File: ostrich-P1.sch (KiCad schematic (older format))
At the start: 112 parts

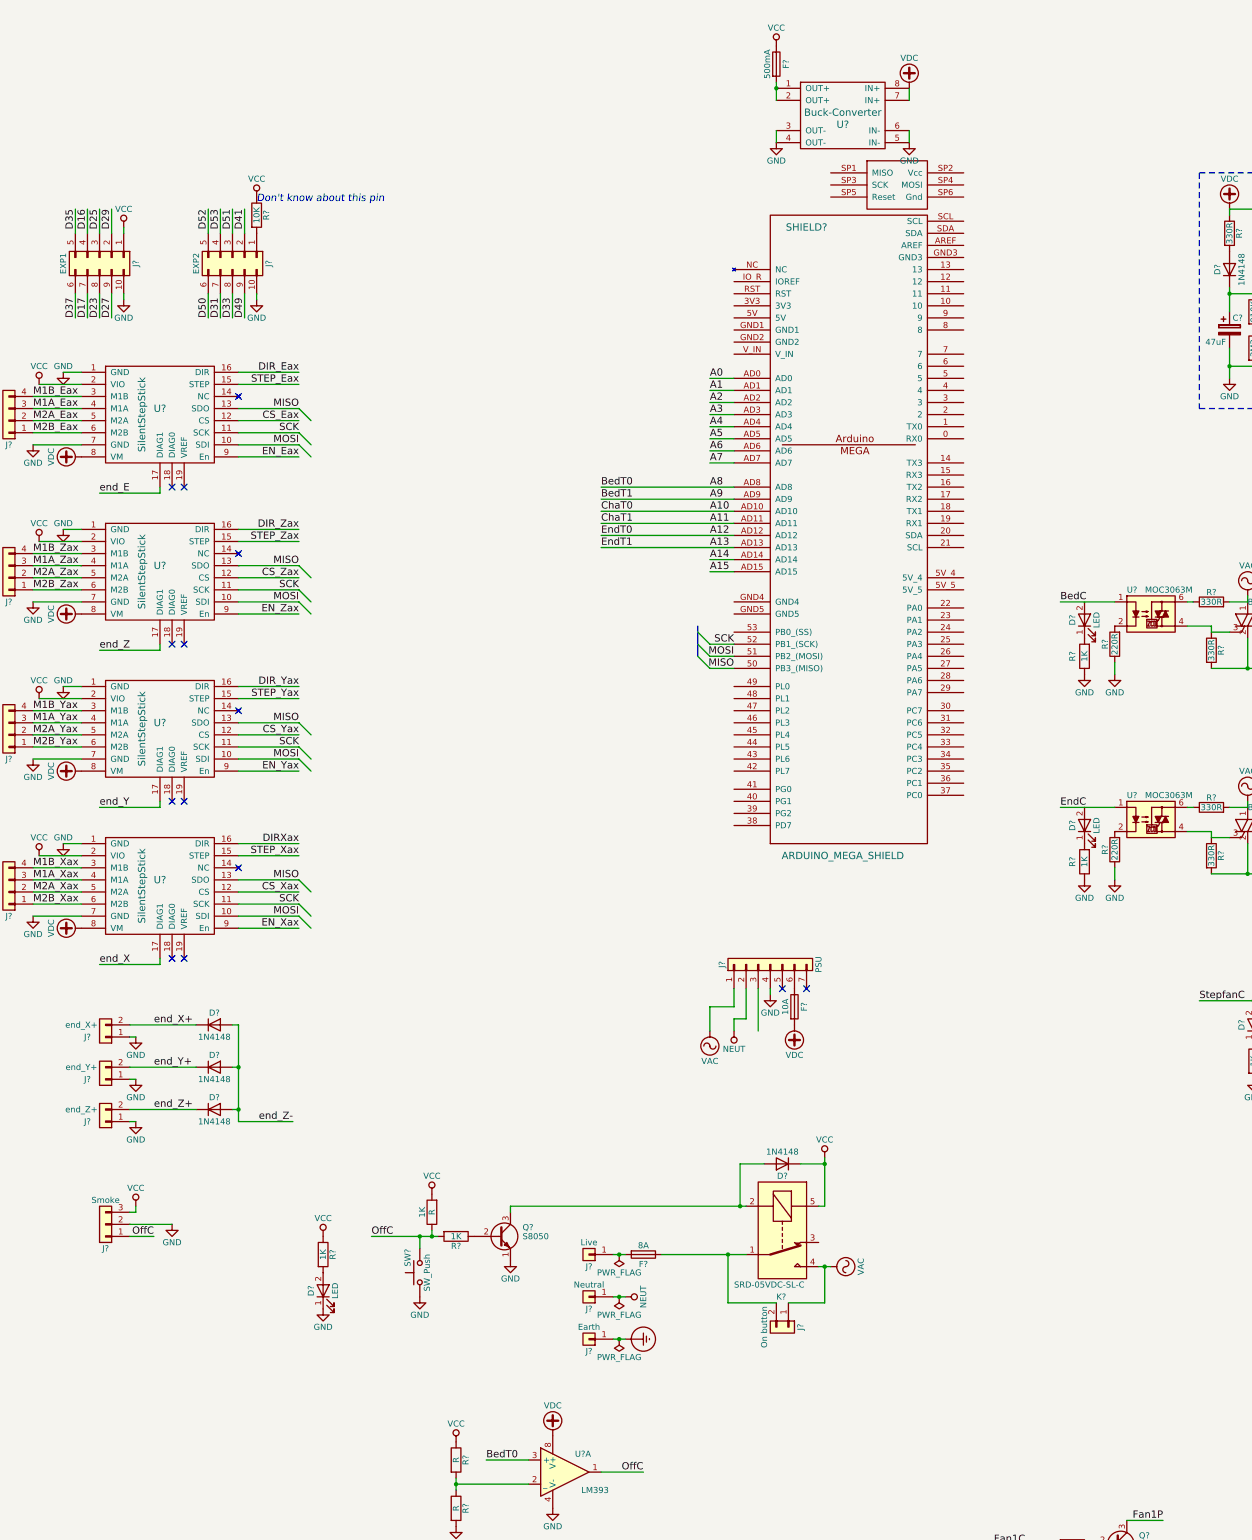
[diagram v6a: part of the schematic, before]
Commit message: switched mega shield library
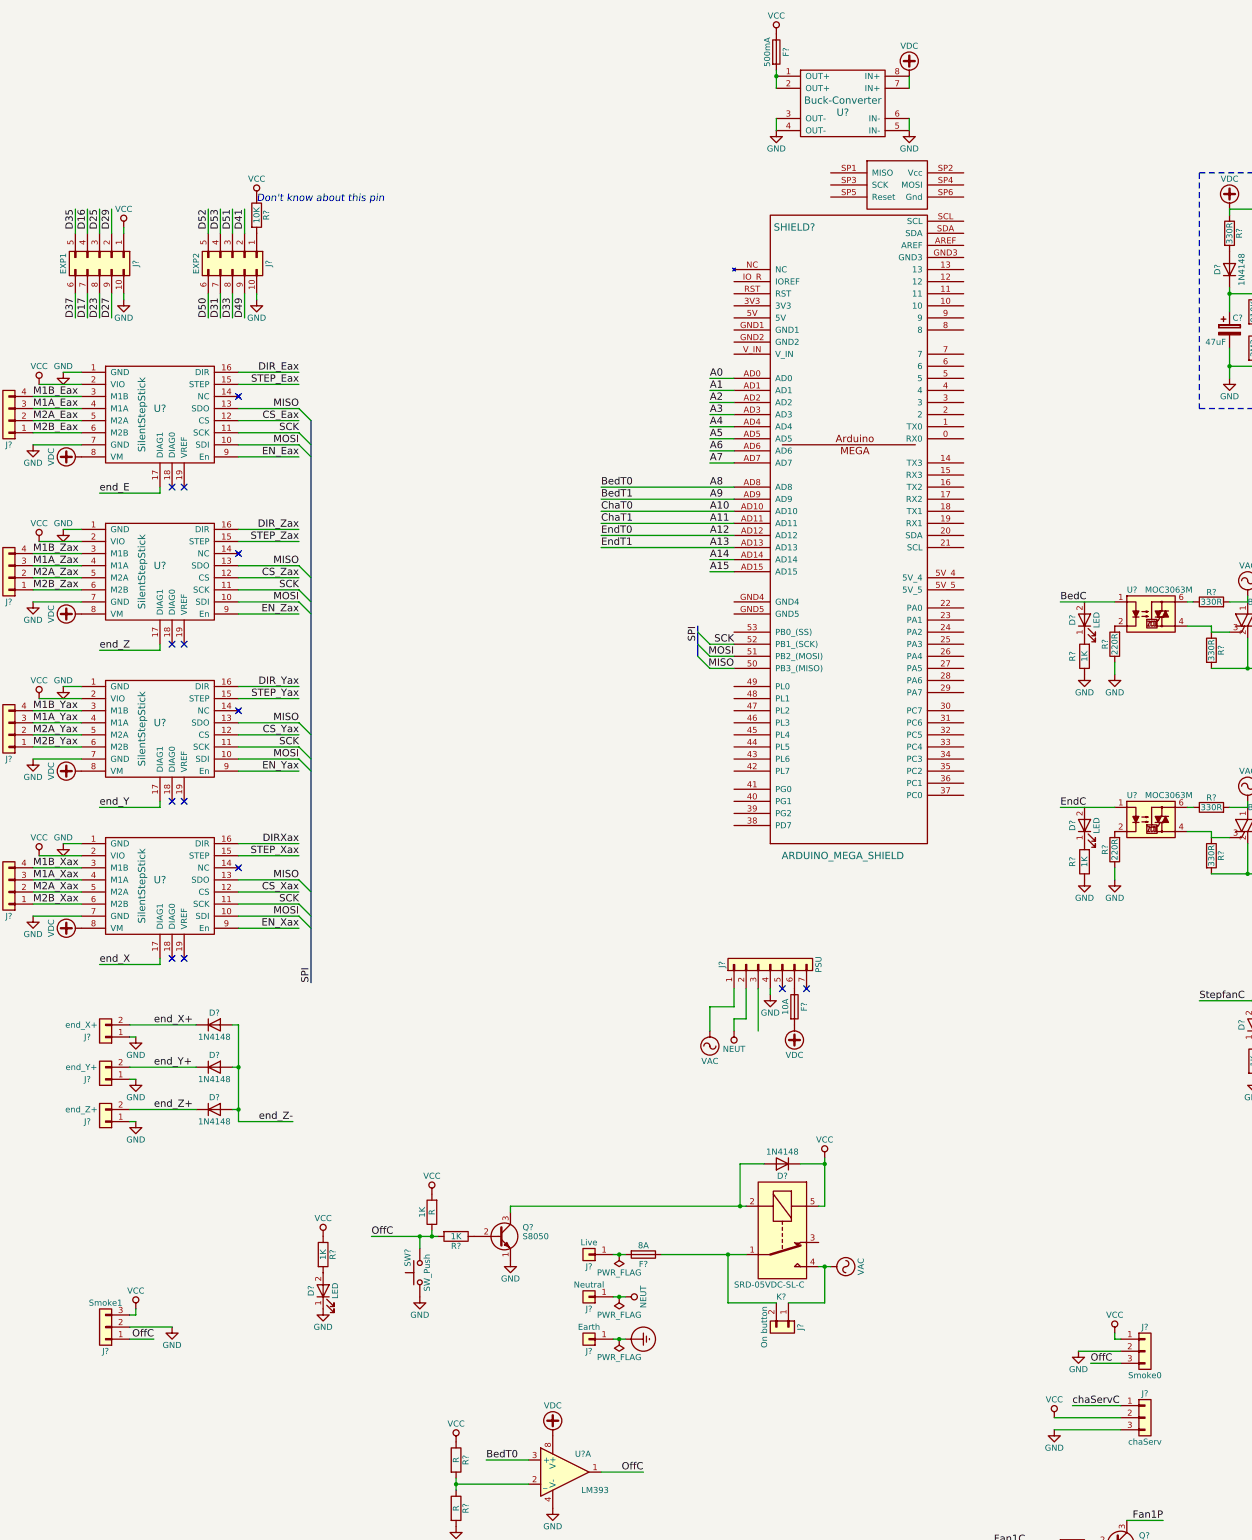
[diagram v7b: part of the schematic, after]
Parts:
- removed SHIELD?: ARDUINO_MEGA_SHIELD, symbol ARDUINO_MEGA_SHIELD
- added J?: Smoke1, symbol Conn_01x03
- added J?: chaServ, symbol Conn_01x03
- added SHIELD?: ARDUINO_MEGA_SHIELD, FT:ARDUINO_MEGA_SHIELD, symbol ARDUINO_MEGA_SHIELD
- J?: value Smoke -> Smoke0
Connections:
- net A0: now also SHIELD?.AD0
- net A1: now also SHIELD?.AD1
- net A10: now also SHIELD?.AD10
- net A11: now also SHIELD?.AD11
- net A12: now also SHIELD?.AD12
- net A13: now also SHIELD?.AD13
- net A14: now also SHIELD?.AD14
- net A15: now also SHIELD?.AD15
- net A2: now also SHIELD?.AD2
- net A3: now also SHIELD?.AD3
- net A4: now also SHIELD?.AD4
- net A5: now also SHIELD?.AD5
- net A6: now also SHIELD?.AD6
- net A7: now also SHIELD?.AD7
- net A8: now also SHIELD?.AD8
- net A9: now also SHIELD?.AD9
- net GND: now also J?.2 (Pin_2), J?.3 (Pin_3)
- net MISO: now also SHIELD?.50 (PB3_(MISO))
- net MOSI: now also SHIELD?.51 (PB2_(MOSI))
- net OffC: now also J?.3 (Pin_3), J?.1 (Pin_1); no longer J?.1 (Pin_1)
- net SCK: now also SHIELD?.52 (PB1_(SCK))
- net VCC: now also J?.1 (Pin_1), J?.2 (Pin_2), J?.3 (Pin_3); no longer J?.3 (Pin_3)
- new net chaServC: J?.1 (Pin_1)
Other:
- moved on the sheet: F?, J?, U?
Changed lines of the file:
@@
 LIBS:contrib
 LIBS:valves
-LIBS:arduino_shieldsNCL
 LIBS:my components
 LIBS:ESP8266
+LIBS:freetronics_schematic
 LIBS:ostrich-P1-cache
 EELAYER 25 0
@@
 $EndDescr
 $Comp
-L ARDUINO_MEGA_SHIELD SHIELD?
-U 1 1 5AF9CD22
-P 6500 3450
-F 0 "SHIELD?" H 6100 5950 60  0000 C CNN
-F 1 "ARDUINO_MEGA_SHIELD" H 6400 750 60  0000 C CNN
-F 2 "" H 6500 3450 60  0001 C CNN
-F 3 "" H 6500 3450 60  0001 C CNN
-	1    6500 3450
-	1    0    0    -1
-$EndComp
-$Comp
 L SilentStepStick U?
 U 1 1 5AF9DD5F
@@
 L Buck-Converter U?
 U 1 1 5AFC21BD
-P 6400 0
-F 0 "U?" H 6400 -100 60  0000 C CNN
-F 1 "Buck-Converter" H 6400 0   60  0000 C CNN
-F 2 "" H 6400 0   60  0001 C CNN
-F 3 "" H 6400 0   60  0001 C CNN
-	1    6400 0
+P 6400 -100
+F 0 "U?" H 6400 -200 60  0000 C CNN
+F 1 "Buck-Converter" H 6400 -100 60  0000 C CNN
+F 2 "" H 6400 -100 60  0001 C CNN
+F 3 "" H 6400 -100 60  0001 C CNN
+	1    6400 -100
 	1    0    0    -1
 $EndComp
@@
 L VDC #PWR030
 U 1 1 5AFC32E0
-P 6950 -200
-F 0 "#PWR030" H 6950 -300 50  0001 C CNN
-F 1 "VDC" H 6950 50  50  0000 C CNN
-F 2 "" H 6950 -200 50  0001 C CNN
-F 3 "" H 6950 -200 50  0001 C CNN
-	1    6950 -200
+P 6950 -300
+F 0 "#PWR030" H 6950 -400 50  0001 C CNN
+F 1 "VDC" H 6950 -50 50  0000 C CNN
+F 2 "" H 6950 -300 50  0001 C CNN
+F 3 "" H 6950 -300 50  0001 C CNN
+	1    6950 -300
 	1    0    0    -1
 $EndComp
@@
 L VCC #PWR031
 U 1 1 5AFC334E
-P 5850 -550
-F 0 "#PWR031" H 5850 -700 50  0001 C CNN
-F 1 "VCC" H 5850 -400 50  0000 C CNN
-F 2 "" H 5850 -550 50  0001 C CNN
-F 3 "" H 5850 -550 50  0001 C CNN
-	1    5850 -550
+P 5850 -650
+F 0 "#PWR031" H 5850 -800 50  0001 C CNN
+F 1 "VCC" H 5850 -500 50  0000 C CNN
+F 2 "" H 5850 -650 50  0001 C CNN
+F 3 "" H 5850 -650 50  0001 C CNN
+	1    5850 -650
 	1    0    0    -1
 $EndComp
@@
 L GND #PWR032
 U 1 1 5AFC33BC
-P 5850 250
-F 0 "#PWR032" H 5850 0   50  0001 C CNN
-F 1 "GND" H 5850 100 50  0000 C CNN
-F 2 "" H 5850 250 50  0001 C CNN
-F 3 "" H 5850 250 50  0001 C CNN
-	1    5850 250
+P 5850 150
+F 0 "#PWR032" H 5850 -100 50  0001 C CNN
+F 1 "GND" H 5850 0   50  0000 C CNN
+F 2 "" H 5850 150 50  0001 C CNN
+F 3 "" H 5850 150 50  0001 C CNN
+	1    5850 150
 	1    0    0    -1
 $EndComp
@@
 L GND #PWR033
 U 1 1 5AFC342A
-P 6950 250
-F 0 "#PWR033" H 6950 0   50  0001 C CNN
-F 1 "GND" H 6950 100 50  0000 C CNN
-F 2 "" H 6950 250 50  0001 C CNN
-F 3 "" H 6950 250 50  0001 C CNN
-	1    6950 250
+P 6950 150
+F 0 "#PWR033" H 6950 -100 50  0001 C CNN
+F 1 "GND" H 6950 0   50  0000 C CNN
+F 2 "" H 6950 150 50  0001 C CNN
+F 3 "" H 6950 150 50  0001 C CNN
+	1    6950 150
 	1    0    0    -1
 $EndComp
@@
 	10250 6050 10500 6050
 Wire Wire Line
-	6950 250  6950 150
+	6950 150  6950 50
 Wire Wire Line
-	6950 -100 6950 -200
+	6950 -200 6950 -300
 Wire Wire Line
-	5850 -250 5850 -100
+	5850 -350 5850 -200
 Wire Wire Line
-	5850 150  5850 250
+	5850 50   5850 150
 Wire Wire Line
 	10500 7050 10450 7050
@@
 L Fuse F?
 U 1 1 5B0086B8
-P 5850 -400
-F 0 "F?" V 5930 -400 50  0000 C CNN
-F 1 "500mA" V 5775 -400 50  0000 C CNN
-F 2 "" V 5780 -400 50  0001 C CNN
-F 3 "" H 5850 -400 50  0001 C CNN
-	1    5850 -400
+P 5850 -500
+F 0 "F?" V 5930 -500 50  0000 C CNN
+F 1 "500mA" V 5775 -500 50  0000 C CNN
+F 2 "" V 5780 -500 50  0001 C CNN
+F 3 "" H 5850 -500 50  0001 C CNN
+	1    5850 -500
 	1    0    0    -1
 $EndComp
-Connection ~ 5850 -200
+Connection ~ 5850 -300
 $Comp
 L Fuse F?
@@
 L Conn_01x03 J?
 U 1 1 5B00C978
-P 300 9200
-F 0 "J?" H 300 9400 50  0000 C CNN
-F 1 "Smoke" H 300 9000 50  0000 C CNN
-F 2 "" H 300 9200 50  0001 C CNN
-F 3 "" H 300 9200 50  0001 C CNN
-	1    300  9200
-	-1   0    0    1
+P 8900 10250
+F 0 "J?" H 8900 10450 50  0000 C CNN
+F 1 "Smoke0" H 8900 10050 50  0000 C CNN
+F 2 "" H 8900 10250 50  0001 C CNN
+F 3 "" H 8900 10250 50  0001 C CNN
+	1    8900 10250
+	1    0    0    -1
 $EndComp
 $Comp
 L VCC #PWR?
 U 1 1 5B00D028
-P 550 9050
-F 0 "#PWR?" H 550 8900 50  0001 C CNN
-F 1 "VCC" H 550 9200 50  0000 C CNN
-F 2 "" H 550 9050 50  0001 C CNN
-F 3 "" H 550 9050 50  0001 C CNN
-	1    550  9050
+P 8650 10100
+F 0 "#PWR?" H 8650 9950 50  0001 C CNN
+F 1 "VCC" H 8650 10250 50  0000 C CNN
+F 2 "" H 8650 10100 50  0001 C CNN
+F 3 "" H 8650 10100 50  0001 C CNN
+	1    8650 10100
 	1    0    0    -1
 $EndComp
@@
 L GND #PWR?
 U 1 1 5B00D10A
-P 850 9200
-F 0 "#PWR?" H 850 8950 50  0001 C CNN
-F 1 "GND" H 850 9050 50  0000 C CNN
-F 2 "" H 850 9200 50  0001 C CNN
-F 3 "" H 850 9200 50  0001 C CNN
-	1    850  9200
+P 8350 10250
+F 0 "#PWR?" H 8350 10000 50  0001 C CNN
+F 1 "GND" H 8350 10100 50  0000 C CNN
+F 2 "" H 8350 10250 50  0001 C CNN
+F 3 "" H 8350 10250 50  0001 C CNN
+	1    8350 10250
 	1    0    0    -1
 $EndComp
 Wire Wire Line
-	500  9100 550  9100
-Wire Wire Line
-	550  9100 550  9050
-Wire Wire Line
-	500  9200 850  9200
+	8450 10350 8700 10350
 Wire Wire Line
-	500  9300 700  9300
-Text Label 700  9300 2    60   ~ 0
+	8700 10250 8350 10250
+Text Label 8450 10350 0    60   ~ 0
 OffC
 Text Label 4400 3400 0    60   ~ 0
@@
 Wire Wire Line
 	4750 13650 4400 13650
+$Comp
+L Conn_01x03 J?
+U 1 1 5B01C29E
+P 300 10050
+F 0 "J?" H 300 10250 50  0000 C CNN
+F 1 "Smoke1" H 300 9850 50  0000 C CNN
+F 2 "" H 300 10050 50  0001 C CNN
+F 3 "" H 300 10050 50  0001 C CNN
+	1    300  10050
+	-1   0    0    1
+$EndComp
+$Comp
+L VCC #PWR?
+U 1 1 5B01C2A4
+P 550 9900
+F 0 "#PWR?" H 550 9750 50  0001 C CNN
+F 1 "VCC" H 550 10050 50  0000 C CNN
+F 2 "" H 550 9900 50  0001 C CNN
+F 3 "" H 550 9900 50  0001 C CNN
+	1    550  9900
+	1    0    0    -1
+$EndComp
+$Comp
+L GND #PWR?
+U 1 1 5B01C2AA
+P 850 10050
+F 0 "#PWR?" H 850 9800 50  0001 C CNN
+F 1 "GND" H 850 9900 50  0000 C CNN
+F 2 "" H 850 10050 50  0001 C CNN
+F 3 "" H 850 10050 50  0001 C CNN
+	1    850  10050
+	1    0    0    -1
+$EndComp
+Wire Wire Line
+	500  9950 550  9950
+Wire Wire Line
+	550  9950 550  9900
+Wire Wire Line
+	500  10050 850  10050
+Wire Wire Line
+	500  10150 700  10150
+Text Label 700  10150 2    60   ~ 0
+OffC
+$Comp
+L Conn_01x03 J?
+U 1 1 5B01D6F8
+P 8900 10800
+F 0 "J?" H 8900 11000 50  0000 C CNN
+F 1 "chaServ" H 8900 10600 50  0000 C CNN
+F 2 "" H 8900 10800 50  0001 C CNN
+F 3 "" H 8900 10800 50  0001 C CNN
+	1    8900 10800
+	1    0    0    -1
+$EndComp
+$Comp
+L VCC #PWR?
+U 1 1 5B01E1EF
+P 8150 10800
+F 0 "#PWR?" H 8150 10650 50  0001 C CNN
+F 1 "VCC" H 8150 10950 50  0000 C CNN
+F 2 "" H 8150 10800 50  0001 C CNN
+F 3 "" H 8150 10800 50  0001 C CNN
+	1    8150 10800
+	1    0    0    -1
+$EndComp
+Wire Wire Line
+	8700 10800 8150 10800
+Text Label 8300 10700 0    60   ~ 0
+chaServC
+Wire Wire Line
+	8300 10700 8700 10700
+$Comp
+L GND #PWR?
+U 1 1 5B01F053
+P 8150 10900
+F 0 "#PWR?" H 8150 10650 50  0001 C CNN
+F 1 "GND" H 8150 10750 50  0000 C CNN
+F 2 "" H 8150 10900 50  0001 C CNN
+F 3 "" H 8150 10900 50  0001 C CNN
+	1    8150 10900
+	1    0    0    -1
+$EndComp
+Wire Wire Line
+	8700 10900 8150 10900
+Wire Wire Line
+	8650 10100 8650 10150
+Wire Wire Line
+	8650 10150 8700 10150
+Wire Bus Line
+	2000 2550 2000 7200
+Text Label 2000 7200 1    60   ~ 0
+SPI
+Text Label 5200 4250 3    60   ~ 0
+SPI
+$Comp
+L ARDUINO_MEGA_SHIELD SHIELD?
+U 1 1 5B027313
+P 6500 3450
+F 0 "SHIELD?" H 6000 5950 60  0000 C CNN
+F 1 "ARDUINO_MEGA_SHIELD" H 6400 750 60  0000 C CNN
+F 2 "FT:ARDUINO_MEGA_SHIELD" H 6500 3250 50  0001 C CNN
+F 3 "" H 6500 3450 60  0000 C CNN
+	1    6500 3450
+	1    0    0    -1
+$EndComp
 $EndSCHEMATC
